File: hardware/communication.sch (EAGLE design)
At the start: 34 parts, among them J1 MICRO_USB_B_HIROSE_ZX62-B-5PA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, SW1 TVAF06-A020B-R, U2 NJM12888F, X1 FA-238

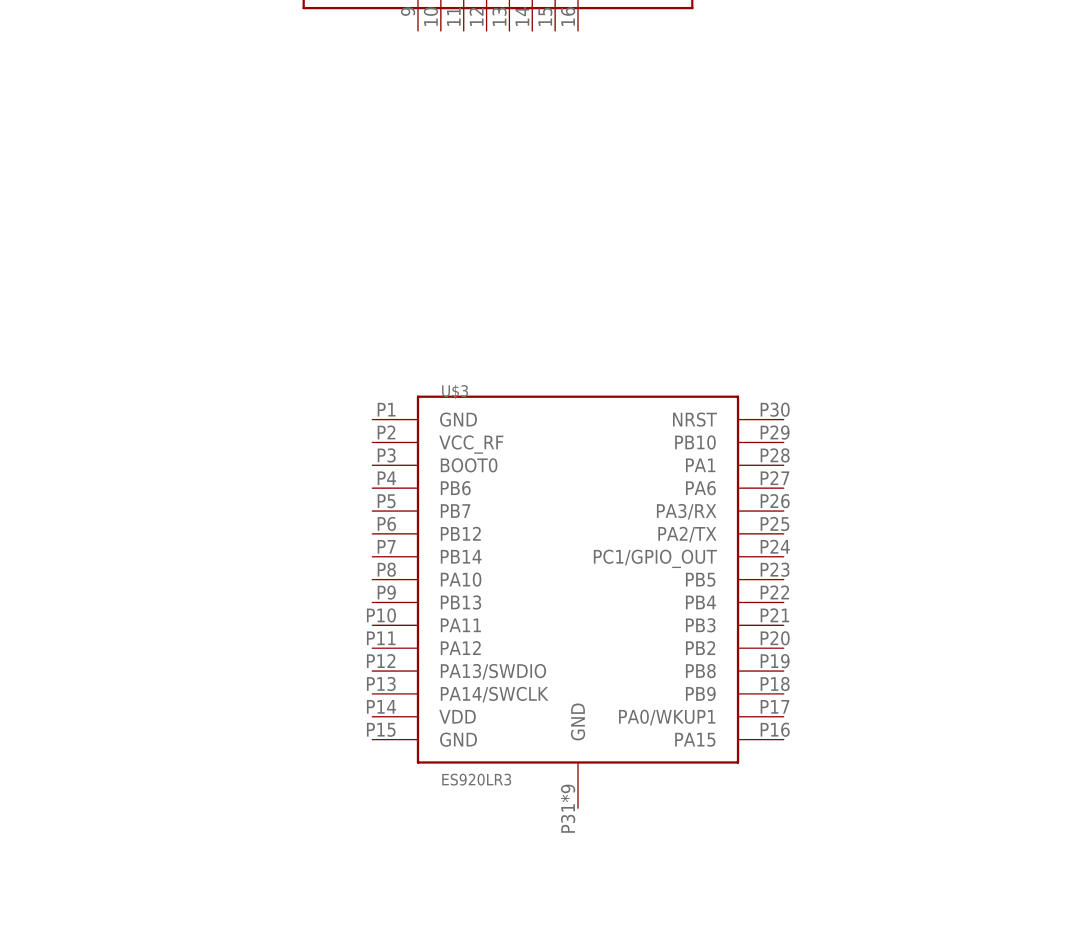
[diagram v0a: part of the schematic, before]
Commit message: communicationの回路図と基盤の途中経過です。Lo-Raの部分が終わって、残りはTweLiteをやれば完成のはずです。初めて基盤の設計をしているので不備が必ずあると思います。確認お願いします。
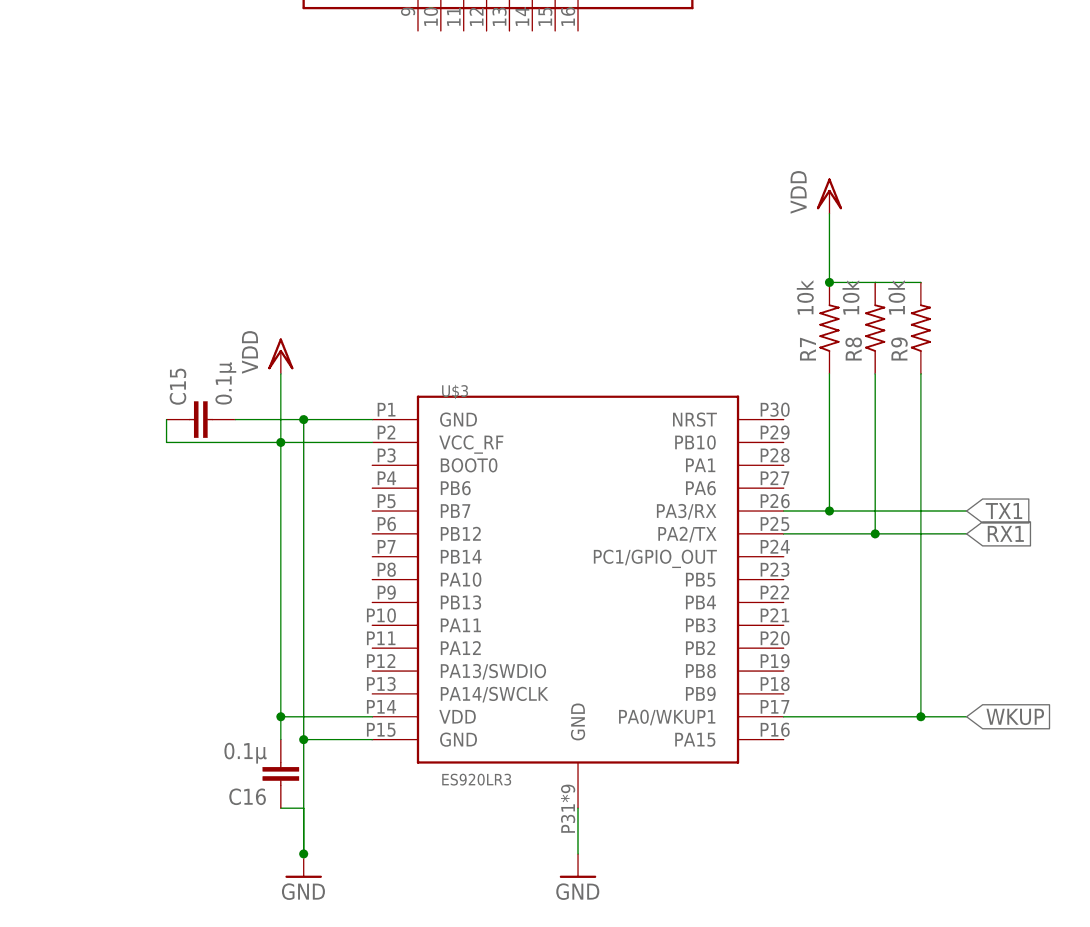
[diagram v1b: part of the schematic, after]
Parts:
- added C15, C16: 0.1µ, rcl:C-EUC0402
- added R7, R8, R9: 10k, rcl:R-US_R0402
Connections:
- new net WKUP: R9.1, U$3.PA0/WKUP1
- net GND: now also C15.2, C16.1, U$3.GND, U$3.GND@1, U$3.GND@2
- net RX1: now also R8.1, U$3.PA2/TX
- net TX1: now also R7.1, U$3.PA3/RX
- net VDD: now also C15.1, C16.2, R7.2, R8.2, R9.2, U$3.VCC_RF, U$3.VDD
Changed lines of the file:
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@@
 <part name="U$1" library="TWELite" deviceset="LITE" device=""/>
 <part name="U$3" library="lora" deviceset="ES920LR3" device=""/>
+<part name="GND1" library="supply1" library_urn="urn:adsk.eagle:library:371" deviceset="GND" device=""/>
+<part name="GND2" library="supply1" library_urn="urn:adsk.eagle:library:371" deviceset="GND" device=""/>
+<part name="VDD1" library="supply1" library_urn="urn:adsk.eagle:library:371" deviceset="VDD" device=""/>
+<part name="C15" library="rcl" library_urn="urn:adsk.eagle:library:334" deviceset="C-EU" device="C0402" package3d_urn="urn:adsk.eagle:package:23626/2" value="0.1µ"/>
+<part name="C16" library="rcl" library_urn="urn:adsk.eagle:library:334" deviceset="C-EU" device="C0402" package3d_urn="urn:adsk.eagle:package:23626/2" value="0.1µ"/>
+<part name="R7" library="rcl" library_urn="urn:adsk.eagle:library:334" deviceset="R-US_" device="R0402" package3d_urn="urn:adsk.eagle:package:23547/3" value="10k"/>
+<part name="R8" library="rcl" library_urn="urn:adsk.eagle:library:334" deviceset="R-US_" device="R0402" package3d_urn="urn:adsk.eagle:package:23547/3" value="10k"/>
+<part name="VDD2" library="supply1" library_urn="urn:adsk.eagle:library:371" deviceset="VDD" device=""/>
+<part name="R9" library="rcl" library_urn="urn:adsk.eagle:library:334" deviceset="R-US_" device="R0402" package3d_urn="urn:adsk.eagle:package:23547/3" value="10k"/>
 </parts>
 <sheets>
@@
 <attribute name="NAME" x="210.82" y="5.08" size="1.27" layer="95"/>
 <attribute name="VALUE" x="210.82" y="-38.1" size="1.27" layer="96"/>
+</instance>
+<instance part="GND1" gate="1" x="226.06" y="-48.26" smashed="yes">
+<attribute name="VALUE" x="223.52" y="-50.8" size="1.778" layer="96"/>
+</instance>
+<instance part="GND2" gate="1" x="195.58" y="-48.26" smashed="yes">
+<attribute name="VALUE" x="193.04" y="-50.8" size="1.778" layer="96"/>
+</instance>
+<instance part="VDD1" gate="G$1" x="193.04" y="10.16" smashed="yes">
+<attribute name="VALUE" x="190.5" y="7.62" size="1.778" layer="96" rot="R90"/>
+</instance>
+<instance part="C15" gate="G$1" x="182.88" y="2.54" smashed="yes" rot="R90">
+<attribute name="NAME" x="182.499" y="4.064" size="1.778" layer="95" rot="R90"/>
+<attribute name="VALUE" x="187.579" y="4.064" size="1.778" layer="96" rot="R90"/>
+</instance>
+<instance part="C16" gate="G$1" x="193.04" y="-38.1" smashed="yes" rot="R180">
+<attribute name="NAME" x="191.516" y="-38.481" size="1.778" layer="95" rot="R180"/>
+<attribute name="VALUE" x="191.516" y="-33.401" size="1.778" layer="96" rot="R180"/>
+</instance>
+<instance part="R7" gate="G$1" x="254" y="12.7" smashed="yes" rot="R90">
+<attribute name="NAME" x="252.5014" y="8.89" size="1.778" layer="95" rot="R90"/>
+<attribute name="VALUE" x="252.222" y="13.97" size="1.778" layer="96" rot="R90"/>
+</instance>
+<instance part="R8" gate="G$1" x="259.08" y="12.7" smashed="yes" rot="R90">
+<attribute name="NAME" x="257.5814" y="8.89" size="1.778" layer="95" rot="R90"/>
+<attribute name="VALUE" x="257.302" y="13.97" size="1.778" layer="96" rot="R90"/>
+</instance>
+<instance part="VDD2" gate="G$1" x="254" y="27.94" smashed="yes">
+<attribute name="VALUE" x="251.46" y="25.4" size="1.778" layer="96" rot="R90"/>
+</instance>
+<instance part="R9" gate="G$1" x="264.16" y="12.7" smashed="yes" rot="R90">
+<attribute name="NAME" x="262.6614" y="8.89" size="1.778" layer="95" rot="R90"/>
+<attribute name="VALUE" x="262.382" y="13.97" size="1.778" layer="96" rot="R90"/>
 </instance>
 </instances>
@@
 <wire x1="40.64" y1="27.94" x2="40.64" y2="25.4" width="0.1524" layer="91"/>
 <pinref part="GND44" gate="1" pin="GND"/>
+</segment>
+<segment>
+<pinref part="GND1" gate="1" pin="GND"/>
+<pinref part="U$3" gate="G$1" pin="GND"/>
+<wire x1="226.06" y1="-45.72" x2="226.06" y2="-40.64" width="0.1524" layer="91"/>
+</segment>
+<segment>
+<pinref part="GND2" gate="1" pin="GND"/>
+<wire x1="195.58" y1="-45.72" x2="195.58" y2="-40.64" width="0.1524" layer="91"/>
+<wire x1="195.58" y1="-40.64" x2="193.04" y2="-40.64" width="0.1524" layer="91"/>
+<pinref part="U$3" gate="G$1" pin="GND@2"/>
+<wire x1="203.2" y1="-33.02" x2="195.58" y2="-33.02" width="0.1524" layer="91"/>
+<wire x1="195.58" y1="-33.02" x2="195.58" y2="-45.72" width="0.1524" layer="91"/>
+<junction x="195.58" y="-45.72"/>
+<pinref part="C16" gate="G$1" pin="1"/>
+<pinref part="U$3" gate="G$1" pin="GND@1"/>
+<wire x1="203.2" y1="2.54" x2="195.58" y2="2.54" width="0.1524" layer="91"/>
+<pinref part="C15" gate="G$1" pin="2"/>
+<wire x1="195.58" y1="2.54" x2="187.96" y2="2.54" width="0.1524" layer="91"/>
+<wire x1="195.58" y1="-33.02" x2="195.58" y2="2.54" width="0.1524" layer="91"/>
+<junction x="195.58" y="-33.02"/>
+<junction x="195.58" y="2.54"/>
 </segment>
 </net>
@@
 <pinref part="VDD8" gate="G$1" pin="VDD"/>
 </segment>
+<segment>
+<pinref part="U$3" gate="G$1" pin="VCC_RF"/>
+<wire x1="180.34" y1="2.54" x2="180.34" y2="0" width="0.1524" layer="91"/>
+<wire x1="180.34" y1="0" x2="193.04" y2="0" width="0.1524" layer="91"/>
+<pinref part="C15" gate="G$1" pin="1"/>
+<pinref part="VDD1" gate="G$1" pin="VDD"/>
+<wire x1="193.04" y1="0" x2="203.2" y2="0" width="0.1524" layer="91"/>
+<wire x1="193.04" y1="7.62" x2="193.04" y2="0" width="0.1524" layer="91"/>
+<junction x="193.04" y="0"/>
+<pinref part="C16" gate="G$1" pin="2"/>
+<pinref part="U$3" gate="G$1" pin="VDD"/>
+<wire x1="193.04" y1="-30.48" x2="193.04" y2="-33.02" width="0.1524" layer="91"/>
+<wire x1="203.2" y1="-30.48" x2="193.04" y2="-30.48" width="0.1524" layer="91"/>
+<wire x1="193.04" y1="0" x2="193.04" y2="-30.48" width="0.1524" layer="91"/>
+<junction x="193.04" y="-30.48"/>
+</segment>
+<segment>
+<pinref part="R7" gate="G$1" pin="2"/>
+<pinref part="R8" gate="G$1" pin="2"/>
+<wire x1="254" y1="17.78" x2="256.54" y2="17.78" width="0.1524" layer="91"/>
+<pinref part="VDD2" gate="G$1" pin="VDD"/>
+<wire x1="256.54" y1="17.78" x2="259.08" y2="17.78" width="0.1524" layer="91"/>
+<wire x1="254" y1="17.78" x2="254" y2="25.4" width="0.1524" layer="91"/>
+<junction x="254" y="17.78"/>
+<pinref part="R9" gate="G$1" pin="2"/>
+<wire x1="264.16" y1="17.78" x2="259.08" y2="17.78" width="0.1524" layer="91"/>
+</segment>
 </net>
 <net name="USB_DM_1" class="0">
@@
 <label x="30.48" y="83.82" size="1.778" layer="95" rot="R180" xref="yes"/>
 </segment>
+<segment>
+<pinref part="U$3" gate="G$1" pin="PA2/TX"/>
+<wire x1="248.92" y1="-10.16" x2="259.08" y2="-10.16" width="0.1524" layer="91"/>
+<label x="269.24" y="-10.16" size="1.778" layer="95" xref="yes"/>
+<pinref part="R8" gate="G$1" pin="1"/>
+<wire x1="259.08" y1="-10.16" x2="269.24" y2="-10.16" width="0.1524" layer="91"/>
+<wire x1="259.08" y1="7.62" x2="259.08" y2="-10.16" width="0.1524" layer="91"/>
+<junction x="259.08" y="-10.16"/>
+</segment>
 </net>
 <net name="TX1" class="0">
@@
 <wire x1="33.02" y1="86.36" x2="30.48" y2="86.36" width="0.1524" layer="91"/>
 <label x="30.48" y="86.36" size="1.778" layer="95" rot="R180" xref="yes"/>
+</segment>
+<segment>
+<pinref part="U$3" gate="G$1" pin="PA3/RX"/>
+<wire x1="248.92" y1="-7.62" x2="254" y2="-7.62" width="0.1524" layer="91"/>
+<label x="269.24" y="-7.62" size="1.778" layer="95" xref="yes"/>
+<pinref part="R7" gate="G$1" pin="1"/>
+<wire x1="254" y1="-7.62" x2="269.24" y2="-7.62" width="0.1524" layer="91"/>
+<wire x1="254" y1="7.62" x2="254" y2="-7.62" width="0.1524" layer="91"/>
+<junction x="254" y="-7.62"/>
 </segment>
 </net>
@@
 </segment>
 </net>
+<net name="WKUP" class="0">
+<segment>
+<pinref part="U$3" gate="G$1" pin="PA0/WKUP1"/>
+<wire x1="248.92" y1="-30.48" x2="264.16" y2="-30.48" width="0.1524" layer="91"/>
+<pinref part="R9" gate="G$1" pin="1"/>
+<wire x1="264.16" y1="-30.48" x2="269.24" y2="-30.48" width="0.1524" layer="91"/>
+<wire x1="264.16" y1="7.62" x2="264.16" y2="-30.48" width="0.1524" layer="91"/>
+<junction x="264.16" y="-30.48"/>
+<label x="269.24" y="-30.48" size="1.778" layer="95" xref="yes"/>
+</segment>
+</net>

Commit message: communicationの層が一応完成しました。確認お願いします
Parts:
- added C17: 0.1µ, rcl:C-EUC0402
- added R10, R13: 10k, rcl:R-US_R0402
- added R11, R12: 1k, rcl:R-US_R0402
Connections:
- removed net SPI0_CS: RP1.GPIO21
- removed net SPI0_MISO: RP1.GPIO20
- removed net SPI0_MOSI: RP1.GPIO19
- removed net SPI0_SCK: RP1.GPIO18
- removed net SPI1_MISO: RP1.GPIO12
- removed net SPI1_MOSI: RP1.GPIO15
- removed net SPI1_SCK: RP1.GPIO14
- new net CTS0: RP1.GPIO18, U$1.DIO5
- new net TWE_PGM: RP1.GPIO20, U$1.DO1
- new net TWE_RESET: R12.1, R12.2, R13.1, RP1.GPIO21, U$1.!RESET!
- new net TWE_SLEEP: R10.2, R11.1, R11.2, RP1.GPIO19, U$1.DIO3
- net GND: now also C17.1, R13.2, U$1.GND@1, U$1.GND@2
- net RX0: now also U$1.DIO6
- net TX0: now also U$1.DIO7
- net VDD: now also C17.2, R10.1, U$1.VCC
- net WKUP: now also RP1.GPIO12

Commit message: Revert "communicationの層が一応完成しました。確認お願いします"
This reverts commit c7c23561daafb7c0ad8373af90d18b3355d51587.
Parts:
- removed C17: 0.1µ, rcl:C-EUC0402
- removed R10, R13: 10k, rcl:R-US_R0402
- removed R11, R12: 1k, rcl:R-US_R0402
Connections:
- removed net CTS0: RP1.GPIO18, U$1.DIO5
- removed net TWE_PGM: RP1.GPIO20, U$1.DO1
- removed net TWE_RESET: R12.1, R12.2, R13.1, RP1.GPIO21, U$1.!RESET!
- removed net TWE_SLEEP: R10.2, R11.1, R11.2, RP1.GPIO19, U$1.DIO3
- new net SPI0_CS: RP1.GPIO21
- new net SPI0_MISO: RP1.GPIO20
- new net SPI0_MOSI: RP1.GPIO19
- new net SPI0_SCK: RP1.GPIO18
- new net SPI1_MISO: RP1.GPIO12
- new net SPI1_MOSI: RP1.GPIO15
- new net SPI1_SCK: RP1.GPIO14
- net GND: no longer C17.1, R13.2, U$1.GND@1, U$1.GND@2
- net RX0: no longer U$1.DIO6
- net TX0: no longer U$1.DIO7
- net VDD: no longer C17.2, R10.1, U$1.VCC
- net WKUP: no longer RP1.GPIO12

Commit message: communication 回路図、基盤　更新
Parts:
- added C17: 0.1µ, rcl:C-EUC0402
- added R10, R11: 10k, rcl:R-US_R0402
- added R12, R13: 1k, rcl:R-US_R0402
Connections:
- removed net I2C_SCL: RP1.GPIO9
- removed net PWM5_A: RP1.GPIO10
- removed net PWM5_B: RP1.GPIO11
- removed net SPI0_MISO: RP1.GPIO20
- removed net SPI0_MOSI: RP1.GPIO19
- removed net SPI0_SCK: RP1.GPIO18
- removed net SPI1_CS: RP1.GPIO13
- removed net SPI1_MISO: RP1.GPIO12
- removed net SPI1_MOSI: RP1.GPIO15
- removed net SPI1_SCK: RP1.GPIO14
- new net ROLA_SCL: R7.1, RP1.GPIO13, U$3.PB8
- new net ROLA_SDA: R8.1, RP1.GPIO12, U$3.PB9
- new net TWE_BPS: RP1.GPIO20, U$1.DIO17
- new net TWE_PGM: RP1.GPIO9, U$1.DO1
- new net TWE_RESET: R11.2, R12.1, R12.2, RP1.GPIO19, U$1.!RESET!
- new net TWE_RTS: RP1.GPIO10, U$1.DIO5
- new net TWE_RTX: RP1.GPIO14, U$1.DIO6
- new net TWE_SLEEP: R10.1, R13.1, R13.2, RP1.GPIO18, U$1.DIO3
- new net TWE_TRX: RP1.GPIO15, U$1.DIO7
- net GND: now also C17.2, R11.1, U$1.GND@1, U$1.GND@2
- net RX1: no longer R8.1, U$3.PA2/TX
- net TX1: no longer R7.1, U$3.PA3/RX
- net VDD: now also C17.1, R10.2, U$1.VCC
- net WKUP: now also RP1.GPIO11
